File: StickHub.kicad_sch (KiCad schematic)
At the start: 98 parts, among them J1 HOST, J2 USB1, J3 USB2, J4 USB3, J5 USB4, J6 USB5, J7 USB6, J8 USB7, J9 EXTGND, U1 MaxLinear_XR22417-48, U2 Dialog_SLG5NT1487V, Y1 12MHz 50ppm 16-20pF

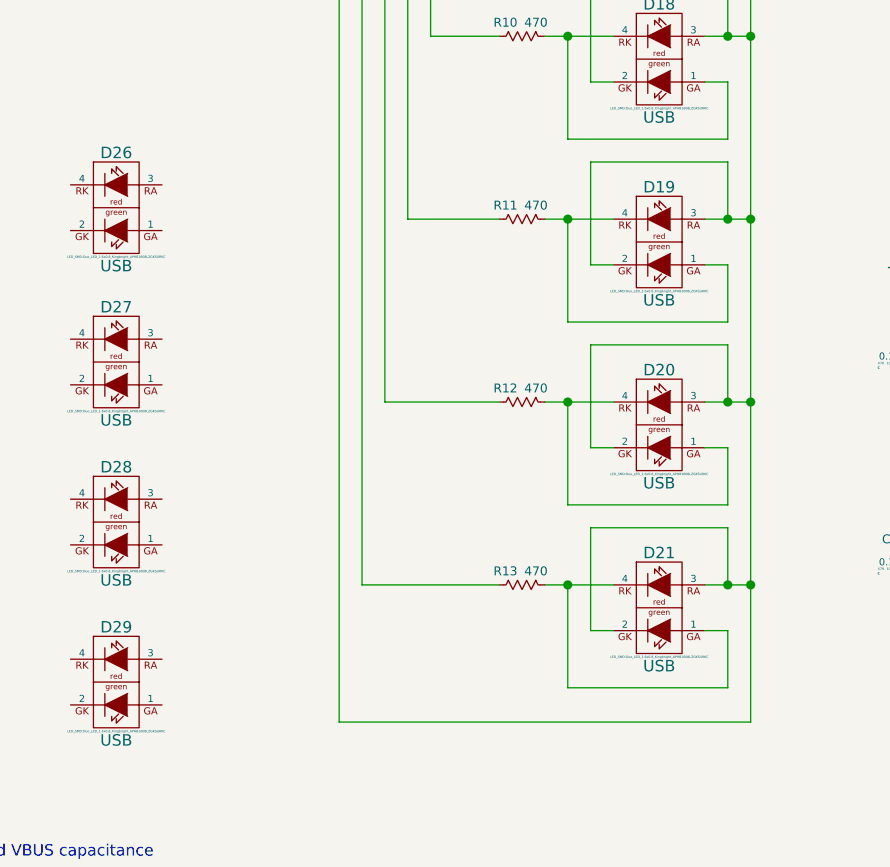
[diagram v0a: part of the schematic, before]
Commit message: wiring LEDs
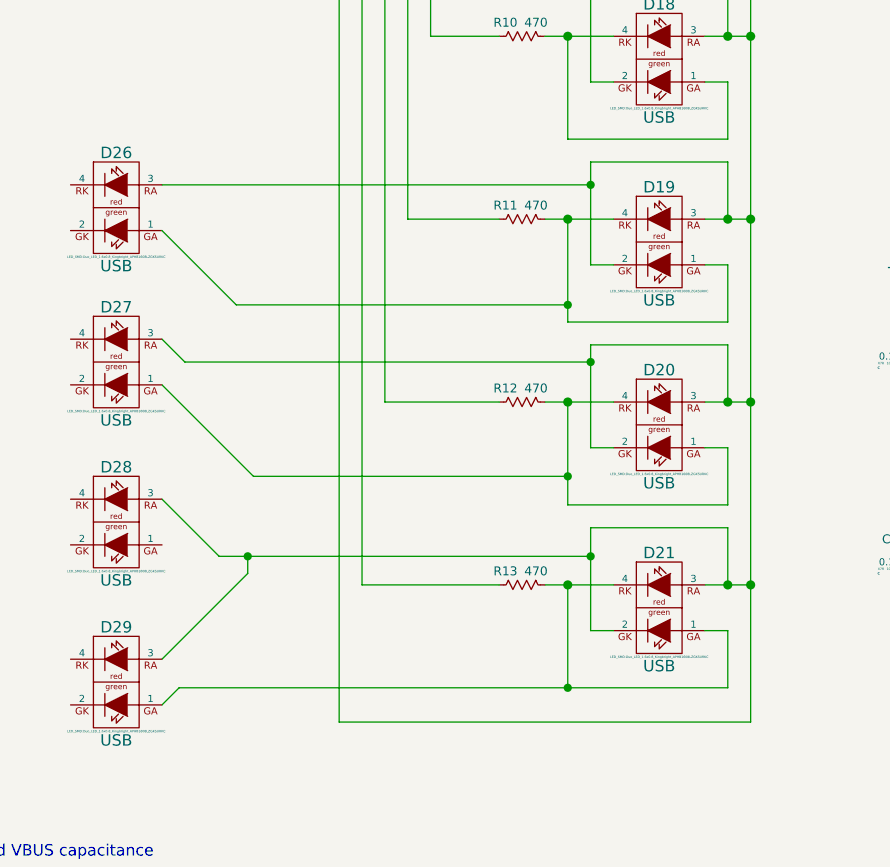
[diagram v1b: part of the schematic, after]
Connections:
- net LC: now also D26.RA (3), D27.RA (3), D28.RA (3), D29.RA (3)
- net at D19.GA (1), D19.RK (4), R11.1: now also D26.GA (1)
- net at D20.GA (1), D20.RK (4), R12.1: now also D27.GA (1)
- net at D21.GA (1), D21.RK (4), R13.1: now also D29.GA (1)
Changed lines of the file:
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@@
   (junction (at 181.61 247.65) (diameter 1.016) (color 0 0 0 0)
   )
+  (junction (at 163.83 222.885) (diameter 0) (color 0 0 0 0)
+  )
   (junction (at 96.52 124.46) (diameter 1.016) (color 0 0 0 0)
   )
+  (junction (at 163.83 244.475) (diameter 0) (color 0 0 0 0)
+  )
   (junction (at 156.21 289.56) (diameter 1.016) (color 0 0 0 0)
   )
@@
   (junction (at 204.47 247.65) (diameter 1.016) (color 0 0 0 0)
   )
+  (junction (at 163.83 203.2) (diameter 0) (color 0 0 0 0)
+  )
+  (junction (at 125.73 244.475) (diameter 0) (color 0 0 0 0)
+  )
   (junction (at 156.21 281.94) (diameter 1.016) (color 0 0 0 0)
   )
@@
   (junction (at 125.73 326.39) (diameter 1.016) (color 0 0 0 0)
   )
+  (junction (at 161.29 259.08) (diameter 0) (color 0 0 0 0)
+  )
   (junction (at 232.41 50.8) (diameter 1.016) (color 0 0 0 0)
   )
@@
   (junction (at 87.63 289.56) (diameter 1.016) (color 0 0 0 0)
   )
+  (junction (at 161.29 235.585) (diameter 0) (color 0 0 0 0)
+  )
   (junction (at 179.07 146.05) (diameter 1.016) (color 0 0 0 0)
   )
@@
   )
   (junction (at 102.87 281.94) (diameter 1.016) (color 0 0 0 0)
+  )
+  (junction (at 161.29 216.535) (diameter 0) (color 0 0 0 0)
   )
   (junction (at 171.45 281.94) (diameter 1.016) (color 0 0 0 0)
@@
     (stroke (width 0) (type solid))
   )
+  (wire (pts (xy 118.745 222.885) (xy 116.205 220.345))
+    (stroke (width 0) (type solid))
+  )
   (wire (pts (xy 73.66 298.45) (xy 73.66 299.72))
     (stroke (width 0) (type solid))
@@
     (stroke (width 0) (type solid))
   )
+  (wire (pts (xy 116.205 203.2) (xy 163.83 203.2))
+    (stroke (width 0) (type solid))
+  )
   (wire (pts (xy 86.36 101.6) (xy 99.06 101.6))
     (stroke (width 0) (type solid))
@@
     (stroke (width 0) (type solid))
   )
+  (wire (pts (xy 163.83 203.2) (xy 163.83 200.66))
+    (stroke (width 0) (type solid))
+  )
   (wire (pts (xy 232.41 93.98) (xy 240.03 93.98))
     (stroke (width 0) (type solid))
@@
     (stroke (width 0) (type solid))
   )
+  (wire (pts (xy 161.29 235.585) (xy 161.29 227.33))
+    (stroke (width 0) (type solid))
+  )
   (wire (pts (xy 158.75 247.65) (xy 161.29 247.65))
     (stroke (width 0) (type solid))
@@
     (stroke (width 0) (type solid))
   )
+  (wire (pts (xy 122.555 244.475) (xy 116.205 238.125))
+    (stroke (width 0) (type solid))
+  )
   (wire (pts (xy 179.07 281.94) (xy 186.69 281.94))
     (stroke (width 0) (type solid))
@@
     (stroke (width 0) (type solid))
   )
+  (wire (pts (xy 124.46 216.535) (xy 116.205 208.28))
+    (stroke (width 0) (type solid))
+  )
+  (wire (pts (xy 125.73 244.475) (xy 122.555 244.475))
+    (stroke (width 0) (type solid))
+  )
   (wire (pts (xy 199.39 240.03) (xy 199.39 241.3))
     (stroke (width 0) (type solid))
@@
     (stroke (width 0) (type solid))
   )
+  (wire (pts (xy 163.83 222.885) (xy 118.745 222.885))
+    (stroke (width 0) (type solid))
+  )
   (wire (pts (xy 176.53 151.13) (xy 179.07 151.13))
     (stroke (width 0) (type solid))
@@
     (stroke (width 0) (type solid))
   )
+  (wire (pts (xy 161.29 216.535) (xy 161.29 207.01))
+    (stroke (width 0) (type solid))
+  )
   (wire (pts (xy 163.83 289.56) (xy 171.45 289.56))
     (stroke (width 0) (type solid))
@@
     (stroke (width 0) (type solid))
   )
+  (wire (pts (xy 163.83 244.475) (xy 125.73 244.475))
+    (stroke (width 0) (type solid))
+  )
   (wire (pts (xy 240.03 72.39) (xy 240.03 69.85))
     (stroke (width 0) (type solid))
@@
     (stroke (width 0) (type solid))
   )
+  (wire (pts (xy 163.83 222.885) (xy 163.83 220.98))
+    (stroke (width 0) (type solid))
+  )
   (wire (pts (xy 110.49 332.74) (xy 110.49 334.01))
     (stroke (width 0) (type solid))
@@
     (stroke (width 0) (type solid))
   )
+  (wire (pts (xy 161.29 259.08) (xy 179.07 259.08))
+    (stroke (width 0) (type solid))
+  )
   (wire (pts (xy 129.54 78.74) (xy 200.66 78.74))
     (stroke (width 0) (type solid))
@@
     (stroke (width 0) (type solid))
   )
+  (wire (pts (xy 125.73 244.475) (xy 125.73 246.38))
+    (stroke (width 0) (type solid))
+  )
   (wire (pts (xy 219.71 50.8) (xy 227.33 50.8))
     (stroke (width 0) (type solid))
@@
     (stroke (width 0) (type solid))
   )
+  (wire (pts (xy 118.11 259.08) (xy 116.205 260.985))
+    (stroke (width 0) (type solid))
+  )
   (wire (pts (xy 87.63 281.94) (xy 87.63 283.21))
     (stroke (width 0) (type solid))
@@
     (stroke (width 0) (type solid))
   )
+  (wire (pts (xy 161.29 235.585) (xy 126.365 235.585))
+    (stroke (width 0) (type solid))
+  )
   (wire (pts (xy 179.07 166.37) (xy 176.53 166.37))
     (stroke (width 0) (type solid))
   )
-  (wire (pts (xy 161.29 238.76) (xy 161.29 227.33))
+  (wire (pts (xy 161.29 238.76) (xy 161.29 235.585))
     (stroke (width 0) (type solid))
   )
@@
     (stroke (width 0) (type solid))
   )
+  (wire (pts (xy 163.83 244.475) (xy 163.83 241.3))
+    (stroke (width 0) (type solid))
+  )
   (wire (pts (xy 52.07 295.91) (xy 45.72 295.91))
     (stroke (width 0) (type solid))
@@
     (stroke (width 0) (type solid))
   )
-  (wire (pts (xy 163.83 252.73) (xy 163.83 241.3))
+  (wire (pts (xy 163.83 252.73) (xy 163.83 244.475))
     (stroke (width 0) (type solid))
   )
@@
     (stroke (width 0) (type solid))
   )
-  (wire (pts (xy 163.83 212.09) (xy 163.83 200.66))
+  (wire (pts (xy 163.83 212.09) (xy 163.83 203.2))
     (stroke (width 0) (type solid))
   )
@@
     (stroke (width 0) (type solid))
   )
-  (wire (pts (xy 163.83 232.41) (xy 163.83 220.98))
+  (wire (pts (xy 163.83 232.41) (xy 163.83 222.885))
     (stroke (width 0) (type solid))
   )
@@
     (stroke (width 0) (type solid))
   )
+  (wire (pts (xy 125.73 246.38) (xy 116.205 255.905))
+    (stroke (width 0) (type solid))
+  )
   (wire (pts (xy 219.71 158.75) (xy 227.33 158.75))
     (stroke (width 0) (type solid))
@@
     (stroke (width 0) (type solid))
   )
-  (wire (pts (xy 179.07 259.08) (xy 161.29 259.08))
+  (wire (pts (xy 118.11 259.08) (xy 161.29 259.08))
     (stroke (width 0) (type solid))
   )
@@
     (stroke (width 0) (type solid))
   )
+  (wire (pts (xy 126.365 235.585) (xy 116.205 225.425))
+    (stroke (width 0) (type solid))
+  )
   (wire (pts (xy 148.59 142.24) (xy 148.59 166.37))
     (stroke (width 0) (type solid))
@@
     (stroke (width 0) (type solid))
   )
+  (wire (pts (xy 161.29 216.535) (xy 124.46 216.535))
+    (stroke (width 0) (type solid))
+  )
   (wire (pts (xy 232.41 72.39) (xy 240.03 72.39))
     (stroke (width 0) (type solid))
@@
     (stroke (width 0) (type solid))
   )
-  (wire (pts (xy 161.29 218.44) (xy 161.29 207.01))
-    (stroke (width 0) (type solid))
-  )
+  (wire (pts (xy 161.29 218.44) (xy 161.29 216.535))
+    (stroke (width 0) (type solid))
+  )

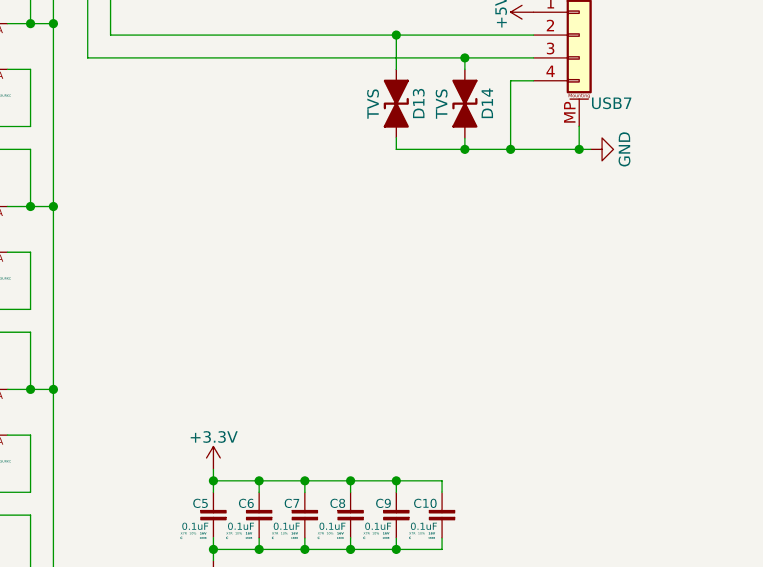
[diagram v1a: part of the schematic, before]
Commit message: adding net and components
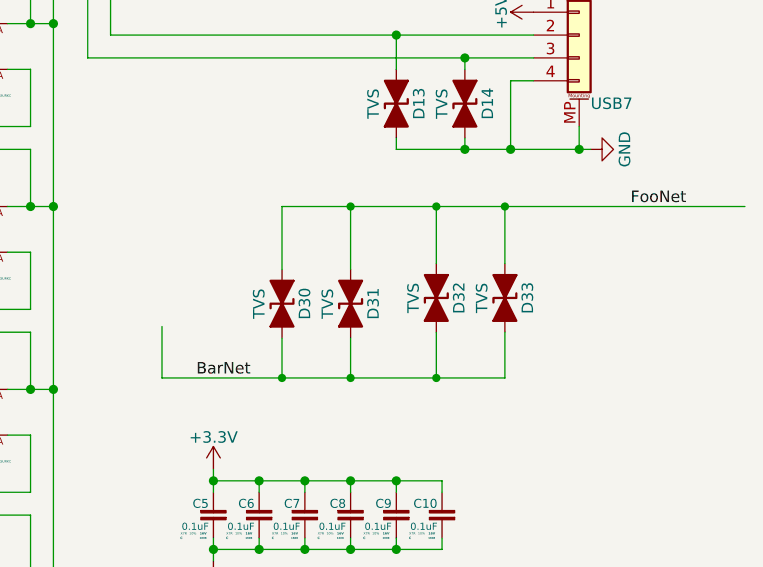
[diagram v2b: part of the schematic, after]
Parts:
- added D30, D31, D32, D33: TVS, Diode_SMD:1006_C, symbol RobotProtos:D_TVS_Filled
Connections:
- new net BarNet: D30.1 (A1), D31.1 (A1), D32.1 (A1), D33.1 (A1)
- new net FooNet: D30.2 (A2), D31.2 (A2), D32.2 (A2), D33.2 (A2)

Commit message: various changes
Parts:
- removed D33: TVS, Diode_SMD:1006_C, symbol RobotProtos:D_TVS_Filled
- added C39, C40: 0.1uF, Capacitor_SMD:1608_C, symbol RobotProtos:Csmall
- D32: footprint Diode_SMD:1006_C -> Diode_SMD:1010_E
- D41: renamed from D31; value TVS -> TVS3
- D45: renamed from D30; value TVS -> TVS2
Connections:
- new net: C39.1, C40.1
- new net: C39.2, C40.2
